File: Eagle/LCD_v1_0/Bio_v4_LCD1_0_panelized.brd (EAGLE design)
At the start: 69.2 x 81.4 mm, 80 parts, among them X1 MINI-USB, X2 16MHz, X3 FH12-08S-1SH, X4 MINI-USB, X5 16MHz, X6 FH12-08S-1SH

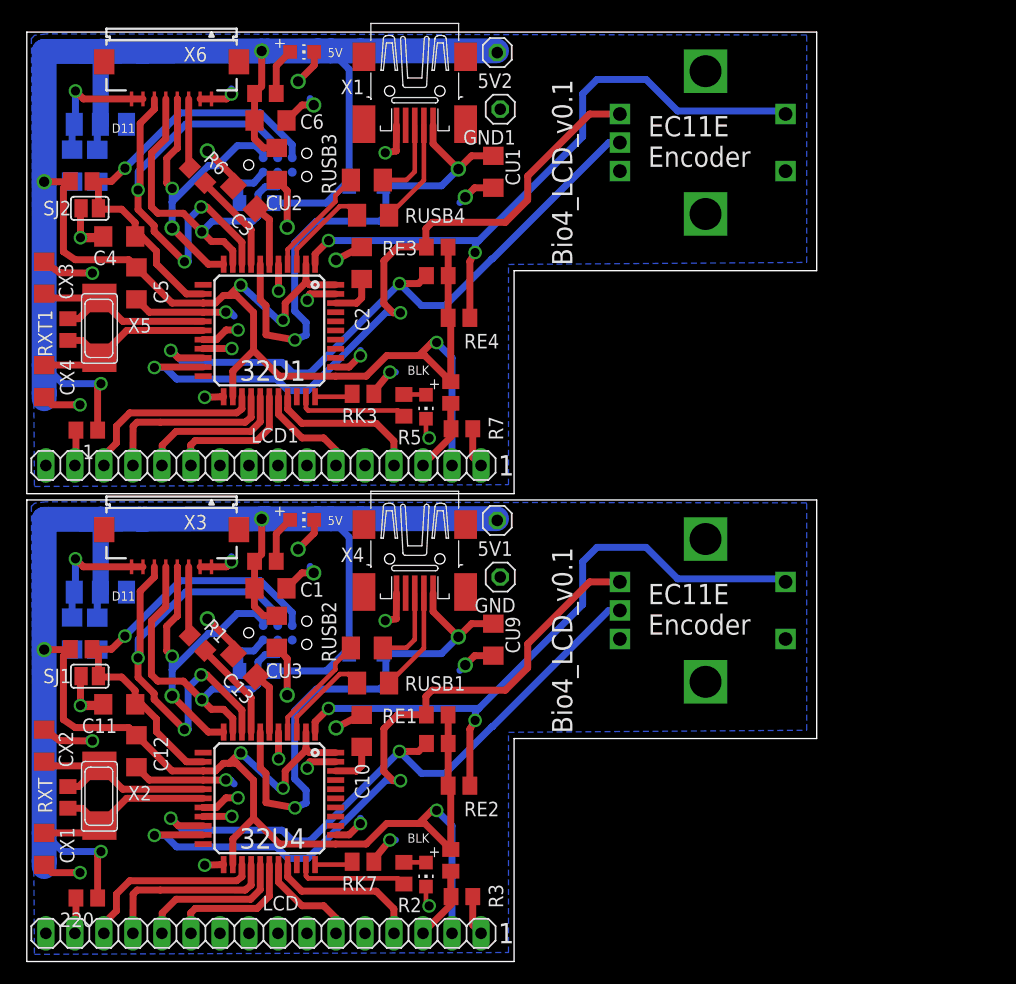
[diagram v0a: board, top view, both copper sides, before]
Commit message: corrected DRC for microcuircuitos on LCD board (0.25mm clearance)
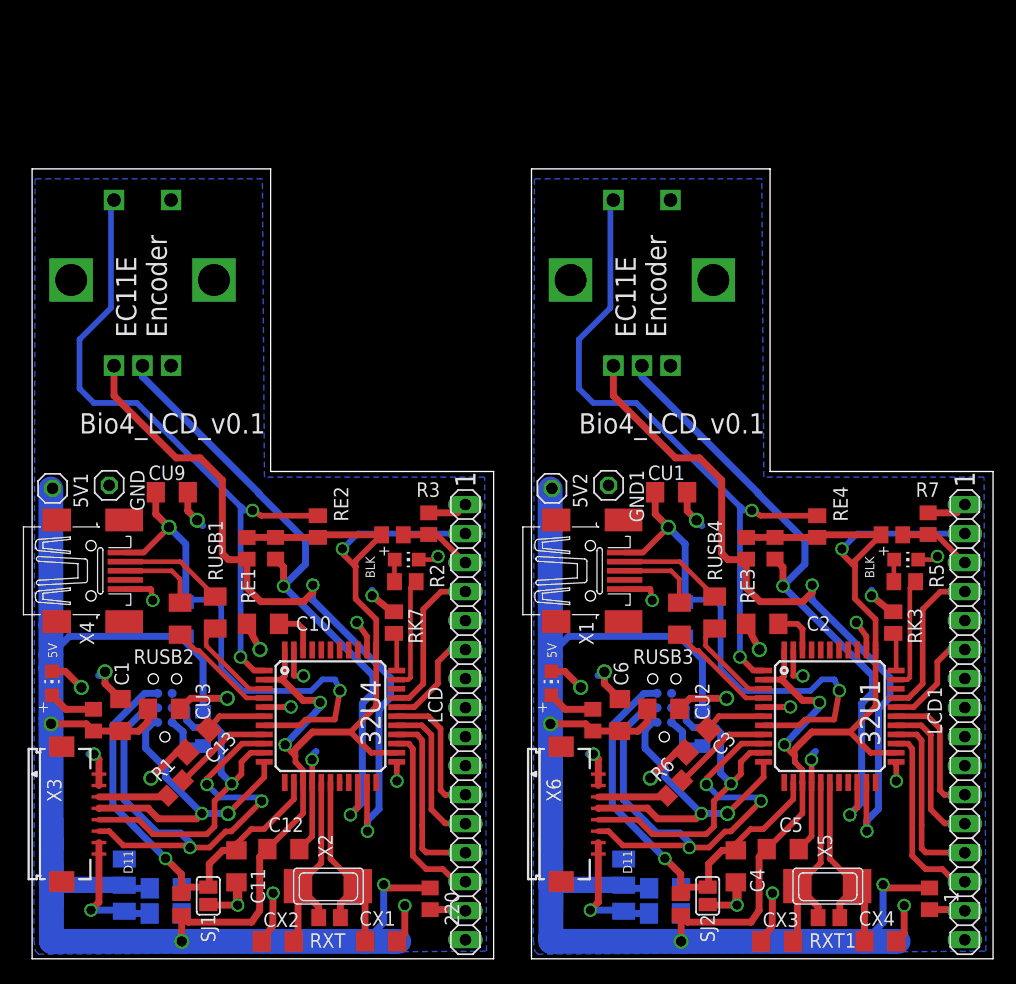
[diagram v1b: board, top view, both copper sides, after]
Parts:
- moved CX4 88.1 mm to (75.0, 1.90), turned to 180 degrees
- moved CX3 86.6 mm to (66.0, 1.89), turned to 0 degrees
- moved 1 84.4 mm to (79.3, 5.63), turned to 270 degrees
- moved RXT1 84.2 mm to (70.5, 3.97), turned to 0 degrees
- moved CU4 83.5 mm to (56.2, 4.34), turned to 180 degrees
- moved RK4 82.2 mm to (57.6, 5.13), turned to 270 degrees
- moved LDO1 81.7 mm to (49.4, 6.84), turned to 270 degrees
- moved SJ2 80.9 mm to (59.9, 5.88), turned to 90 degrees
- moved CU7 80.5 mm to (56.2, 6.54), turned to 180 degrees
- moved X5 80.3 mm to (70.4, 6.73), turned to 180 degrees
- moved C4 77.2 mm to (62.4, 8.47), turned to 270 degrees
- moved C5 75.2 mm to (66.5, 9.97), turned to 180 degrees
- moved X6 74.2 mm to (47.1, 13.0), turned to 270 degrees
- moved R6 68.0 mm to (57.0, 15.3), turned to 45 degrees
- moved LCD1 65.4 mm to (82.4, 21.1), turned to 270 degrees
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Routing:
- net SCL1: track 3.58 -> 0.01 mm, vias 1 -> 0
- net SCL: track 3.58 -> 0.01 mm, vias 1 -> 0
- net SDA1: track 2.56 -> 0.00 mm, vias 1 -> 0
- net SDA: track 2.56 -> 0.00 mm, vias 1 -> 0
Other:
- board size 69.2 x 81.4 mm -> 84.1 x 69.2 mm
